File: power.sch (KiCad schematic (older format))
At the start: 11 parts, among them J9 USB_B, SW1 SW_SPST, SW2 SW_Push, U4 TC1262-33

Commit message: Add a push button power switch.
Also moved reset into the corner and tidied up a few tracks.
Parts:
- removed SW1: SW_SPST, Connector_PinHeader_2.54mm:PinHeader_1x02_P2.54mm_Vertical, symbol Switch:SW_SPST
- added SW1: SW_Push_DPDT, Neotron 32:PHB2UEETS1A, symbol Switch:SW_Push_DPDT
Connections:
- wire segments 37 -> 45
- no-connect marks 2 -> 4
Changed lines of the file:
@@
 	2950 3900 2950 3950
-Wire Wire Line
-	4050 3300 4550 3300
 Wire Wire Line
 	8350 3700 8450 3700
@@
 Text Notes 5150 2950 2    50   ~ 0
 Input Protection
-Text Notes 4150 2950 2    50   ~ 0
+Text Notes 4075 2700 2    50   ~ 0
 Power Switch
 Text Notes 3400 2950 2    50   ~ 0
@@
 	6100 3300 6350 3300
 $Comp
-L Switch:SW_SPST SW1
-U 1 1 5DFA9474
-P 3850 3300
-F 0 "SW1" H 3850 3535 50  0000 C CNN
-F 1 "SW_SPST" H 3850 3444 50  0000 C CNN
-F 2 "Connector_PinHeader_2.54mm:PinHeader_1x02_P2.54mm_Vertical" H 3850 3300 50  0001 C CNN
-F 3 "~" H 3850 3300 50  0001 C CNN
-F 4 "Harwin" H 3850 3300 50  0001 C CNN "Manufacturer"
-F 5 "M20-9990246" H 3850 3300 50  0001 C CNN "PartNo"
-	1    3850 3300
-	1    0    0    -1
-$EndComp
-Wire Wire Line
-	3350 3300 3650 3300
-$Comp
 L Device:R R28
 U 1 1 5E09309F
@@
 Text Notes 550  7700 0    50   Italic 0
 Connect to a 5V USB Power Supply. The board should only use around 100 mA in operation, so almost any USB 'phone charger'\nshould work, provided you have a full-size USB B cable (rather than USB micro-B). We use the full-size B as it is easier to solder the\nconnector.\n\nWe have our own 3.3V LDO to avoid overloading the LDO on the Launchpad.\n\nTaking the RESET pin low should reset the Launchpad, the AtMega and the MCP23S17.
+$Comp
+L Switch:SW_Push_DPDT SW1
+U 1 1 5E119D70
+P 3825 3300
+F 0 "SW1" H 3825 3785 50  0000 C CNN
+F 1 "SW_Push_DPDT" H 3825 3694 50  0000 C CNN
+F 2 "Neotron 32:PHB2UEETS1A" H 3825 3500 50  0001 C CNN
+F 3 "~" H 3825 3500 50  0001 C CNN
+	1    3825 3300
+	1    0    0    -1
+$EndComp
+Wire Wire Line
+	3350 3300 3525 3300
+Wire Wire Line
+	3525 3300 3525 3100
+Wire Wire Line
+	3525 3100 3625 3100
+Wire Wire Line
+	3625 3500 3525 3500
+Wire Wire Line
+	3525 3500 3525 3300
+Connection ~ 3525 3300
+Wire Wire Line
+	4250 3200 4250 3300
+Wire Wire Line
+	4250 3300 4550 3300
+Wire Wire Line
+	4025 3200 4250 3200
+Wire Wire Line
+	4025 3600 4250 3600
+Wire Wire Line
+	4250 3600 4250 3300
+Connection ~ 4250 3300
+NoConn ~ 4025 3400
+NoConn ~ 4025 3000
 $EndSCHEMATC

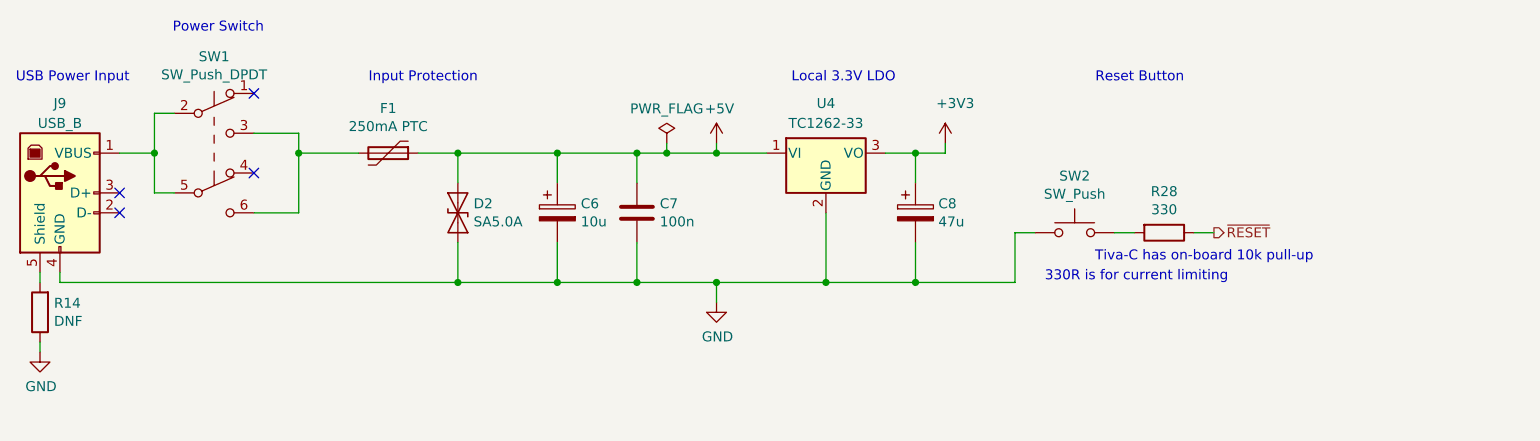
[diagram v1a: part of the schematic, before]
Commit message: Added Reset switch.
Also added 3D models.
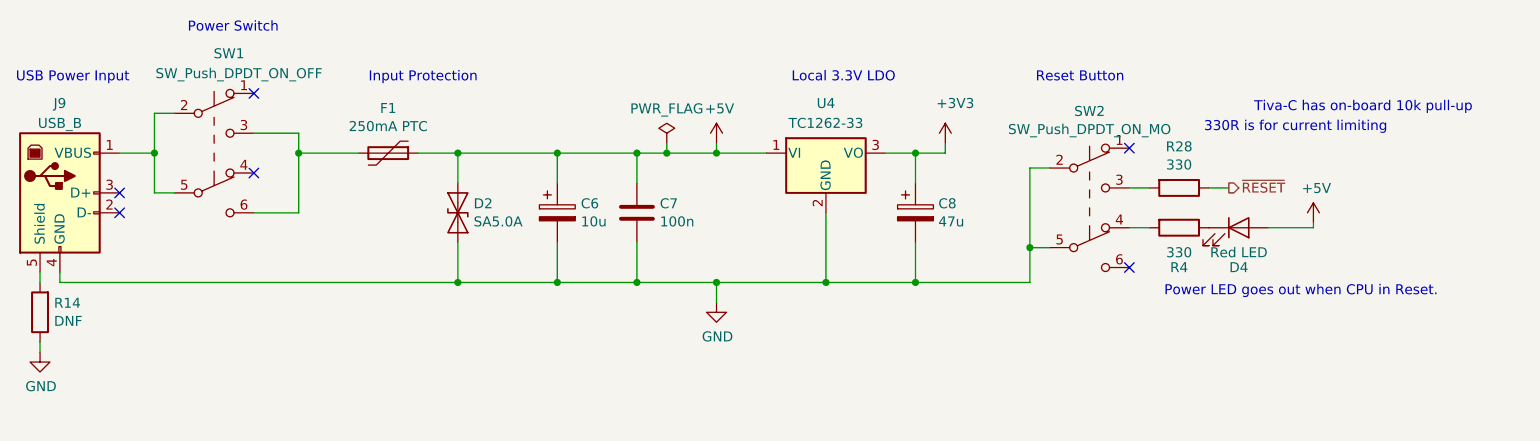
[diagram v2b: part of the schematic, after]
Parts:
- removed SW2: SW_Push, Connector_PinHeader_2.54mm:PinHeader_1x02_P2.54mm_Vertical, symbol Switch:SW_Push
- added D4: Red LED, LED_THT:LED_D3.0mm, symbol Device:LED
- added R4: 330, Resistor_THT:R_Axial_DIN0207_L6.3mm_D2.5mm_P10.16mm_Horizontal, symbol Device:R
- added SW2: SW_Push_DPDT_ON_MO, Neotron 32:PHB2UEETS1A, symbol Switch:SW_Push_DPDT
- SW1: value SW_Push_DPDT -> SW_Push_DPDT_ON_OFF; Manufacturer (none) -> C&K; PartNo (none) -> PHB2UEETS1A
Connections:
- net +5V: now also D4.2 (A)
- net GND: now also SW2.2 (B), SW2.5 (B)
- net at R28.2: now also SW2.3 (C)
- new net: R4.2, SW2.4 (A)
- new net: D4.1 (K), R4.1
- no-connect marks 4 -> 6
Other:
- note added: "Power LED goes out when CPU in Reset."
- moved on the sheet: R28
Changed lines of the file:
@@
 Comment4 ""
 $EndDescr
-Text HLabel 8850 3700 2    50   Output ~ 0
+Text HLabel 8925 3475 2    50   Output ~ 0
 ~RESET
 $Comp
@@
 	1    0    0    -1
 $EndComp
-$Comp
-L Switch:SW_Push SW2
-U 1 1 5DFD5E14
-P 8150 3700
-F 0 "SW2" H 8150 3985 50  0000 C CNN
-F 1 "SW_Push" H 8150 3894 50  0000 C CNN
-F 2 "Connector_PinHeader_2.54mm:PinHeader_1x02_P2.54mm_Vertical" H 8150 3900 50  0001 C CNN
-F 3 "~" H 8150 3900 50  0001 C CNN
-F 4 "Harwin" H 8150 3700 50  0001 C CNN "Manufacturer"
-F 5 "M20-9990246" H 8150 3700 50  0001 C CNN "PartNo"
-	1    8150 3700
-	1    0    0    -1
-$EndComp
 Wire Wire Line
 	3050 3900 3050 3950
@@
 	2950 3900 2950 3950
 Wire Wire Line
-	8350 3700 8450 3700
-Text Notes 8700 2950 2    50   ~ 0
+	8425 3475 8525 3475
+Text Notes 8400 2950 2    50   ~ 0
 Reset Button
 Text Notes 5150 2950 2    50   ~ 0
 Input Protection
-Text Notes 4075 2700 2    50   ~ 0
+Text Notes 4150 2700 2    50   ~ 0
 Power Switch
 Text Notes 3400 2950 2    50   ~ 0
@@
 	7350 3300 7350 3450
 Wire Wire Line
-	7350 3750 7350 3950
-Wire Wire Line
 	6900 3600 6900 3950
 Wire Wire Line
 	6900 3950 7350 3950
 Wire Wire Line
-	7950 3700 7850 3700
-Wire Wire Line
-	7850 3700 7850 3950
-Wire Wire Line
-	7850 3950 7350 3950
-Connection ~ 7350 3950
+	8025 3375 7925 3375
 Wire Wire Line
 	5950 3950 6350 3950
@@
 Wire Wire Line
 	3050 3950 5050 3950
-Text Notes 9350 3850 2    50   ~ 0
+Text Notes 10150 3100 2    50   ~ 0
 Tiva-C has on-board 10k pull-up
 Wire Wire Line
@@
 L Device:R R28
 U 1 1 5E09309F
-P 8600 3700
-F 0 "R28" V 8393 3700 50  0000 C CNN
-F 1 "330" V 8484 3700 50  0000 C CNN
-F 2 "Resistor_THT:R_Axial_DIN0207_L6.3mm_D2.5mm_P10.16mm_Horizontal" V 8530 3700 50  0001 C CNN
-F 3 "~" H 8600 3700 50  0001 C CNN
-F 4 "Stackpole Electronics Inc" H 8600 3700 50  0001 C CNN "Manufacturer"
-F 5 "CF14JT330R" H 8600 3700 50  0001 C CNN "PartNo"
-	1    8600 3700
+P 8675 3475
+F 0 "R28" V 8468 3475 50  0000 C CNN
+F 1 "330" V 8559 3475 50  0000 C CNN
+F 2 "Resistor_THT:R_Axial_DIN0207_L6.3mm_D2.5mm_P10.16mm_Horizontal" V 8605 3475 50  0001 C CNN
+F 3 "~" H 8675 3475 50  0001 C CNN
+F 4 "Stackpole Electronics Inc" H 8675 3475 50  0001 C CNN "Manufacturer"
+F 5 "CF14JT330R" H 8675 3475 50  0001 C CNN "PartNo"
+	1    8675 3475
 	0    1    1    0
 $EndComp
 Wire Wire Line
-	8750 3700 8850 3700
-Text Notes 8000 3950 0    50   ~ 0
+	8825 3475 8925 3475
+Text Notes 8800 3200 0    50   ~ 0
 330R is for current limiting
 Text Notes 550  7700 0    50   Italic 0
@@
 U 1 1 5E119D70
 P 3825 3300
-F 0 "SW1" H 3825 3785 50  0000 C CNN
-F 1 "SW_Push_DPDT" H 3825 3694 50  0000 C CNN
+F 0 "SW1" H 3900 3800 50  0000 C CNN
+F 1 "SW_Push_DPDT_ON_OFF" H 3950 3700 50  0000 C CNN
 F 2 "Neotron 32:PHB2UEETS1A" H 3825 3500 50  0001 C CNN
 F 3 "~" H 3825 3500 50  0001 C CNN
+F 4 "C&K" H 3825 3300 50  0001 C CNN "Manufacturer"
+F 5 "PHB2UEETS1A" H 3825 3300 50  0001 C CNN "PartNo"
 	1    3825 3300
 	1    0    0    -1
@@
 NoConn ~ 4025 3400
 NoConn ~ 4025 3000
+$Comp
+L Switch:SW_Push_DPDT SW2
+U 1 1 5E11D73E
+P 8225 3575
+F 0 "SW2" H 8225 4060 50  0000 C CNN
+F 1 "SW_Push_DPDT_ON_MO" H 8225 3969 50  0000 C CNN
+F 2 "Neotron 32:PHB2UEETS1A" H 8225 3775 50  0001 C CNN
+F 3 "~" H 8225 3775 50  0001 C CNN
+F 4 "C&K" H 8225 3575 50  0001 C CNN "Manufacturer"
+F 5 "PHB2UOATS1A" H 8225 3575 50  0001 C CNN "PartNo"
+	1    8225 3575
+	1    0    0    -1
+$EndComp
+NoConn ~ 8425 3275
+NoConn ~ 8425 3875
+Wire Wire Line
+	7925 3375 7925 3775
+Wire Wire Line
+	8025 3775 7925 3775
+Connection ~ 7925 3775
+$Comp
+L Device:LED D4
+U 1 1 5E12B86C
+P 8975 3675
+F 0 "D4" H 8975 3475 50  0000 C CNN
+F 1 "Red LED" H 8975 3550 50  0000 C CNN
+F 2 "LED_THT:LED_D3.0mm" H 8975 3675 50  0001 C CNN
+F 3 "~" H 8975 3675 50  0001 C CNN
+F 4 "Würth Elektronik" H 8975 3675 50  0001 C CNN "Manufacturer"
+F 5 "151031SS04000" H 8975 3675 50  0001 C CNN "PartNo"
+	1    8975 3675
+	1    0    0    -1
+$EndComp
+Wire Wire Line
+	8425 3675 8525 3675
+$Comp
+L Device:R R4
+U 1 1 5E12DD30
+P 8675 3675
+F 0 "R4" V 8875 3675 50  0000 C CNN
+F 1 "330" V 8800 3675 50  0000 C CNN
+F 2 "Resistor_THT:R_Axial_DIN0207_L6.3mm_D2.5mm_P10.16mm_Horizontal" V 8605 3675 50  0001 C CNN
+F 3 "~" H 8675 3675 50  0001 C CNN
+F 4 "Stackpole Electronics Inc" H 8675 3675 50  0001 C CNN "Manufacturer"
+F 5 "CF14JT330R" H 8675 3675 50  0001 C CNN "PartNo"
+	1    8675 3675
+	0    1    1    0
+$EndComp
+$Comp
+L power:+5V #PWR?
+U 1 1 5E12E57E
+P 9350 3650
+F 0 "#PWR?" H 9350 3500 50  0001 C CNN
+F 1 "+5V" H 9365 3823 50  0000 C CNN
+F 2 "" H 9350 3650 50  0001 C CNN
+F 3 "" H 9350 3650 50  0001 C CNN
+	1    9350 3650
+	1    0    0    -1
+$EndComp
+Wire Wire Line
+	9125 3675 9350 3675
+Wire Wire Line
+	9350 3675 9350 3650
+Text Notes 8600 4025 0    50   ~ 0
+Power LED goes out when CPU in Reset.
+Wire Wire Line
+	7350 3750 7350 3950
+Wire Wire Line
+	7350 3950 7925 3950
+Wire Wire Line
+	7925 3775 7925 3950
+Connection ~ 7350 3950
 $EndSCHEMATC
